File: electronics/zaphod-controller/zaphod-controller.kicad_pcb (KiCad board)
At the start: 4 copper layers, 199.9 x 69.3 mm, 223 parts, among them P1 MOLEX_43160-0102, P11 MOLEX_MINIFIT_JR_2x4_WAY, P12 MOLEX_MINIFIT_JR_2x4_WAY, P13 MOLEX_MINIFIT_JR_2x4_WAY, P14 MOLEX_MINIFIT_JR_2x4_WAY, P15 MOLEX_NANOFIT_2x4_WAY, P17 CONN_01X02, P18 CONN_01X02, P19 CONN_01X02, P2 MOLEX_MINIFIT_JR_2x2_WAY, P20 CONN_01X06, P22 CONN_01X02, P23 MOLEX_KK2.54_1x4_WAY_FAN, P3 MOLEX_MINIFIT_JR_2x2_WAY, P4 MOLEX_MINIFIT_JR_2x2_WAY, P5 MOLEX_MINIFIT_JR_2x2_WAY, Q1 Si7852DP, Q2 Si7852DP, Q3 2N7002P, Q4 NTR1P02T1G, Q5 BC847B, Q6 2N7002P, SW1 B3U-1000P_SPST-NO_SMD, SW2 B3U-1000P_SPST-NO_SMD, SW3 B3U-1000P_SPST-NO_SMD, U1 ISL85410FRZ, U10 ULN2003A, U11 ULN2003A, U2 LM5116, U3 ISL85410FRZ, U4 STM32F429VET6, U5 USBLC6, U6 ACS711KEXLT_15AB, U7 ACS711KEXLT_15AB, U8 ACS711KEXLT_15AB, U9 ACS711KEXLT_15AB, X1 CSTCE8M00G55Z, X2 SWD_SMT_SOCKET, X3 ABS06-107-32.768KHZ

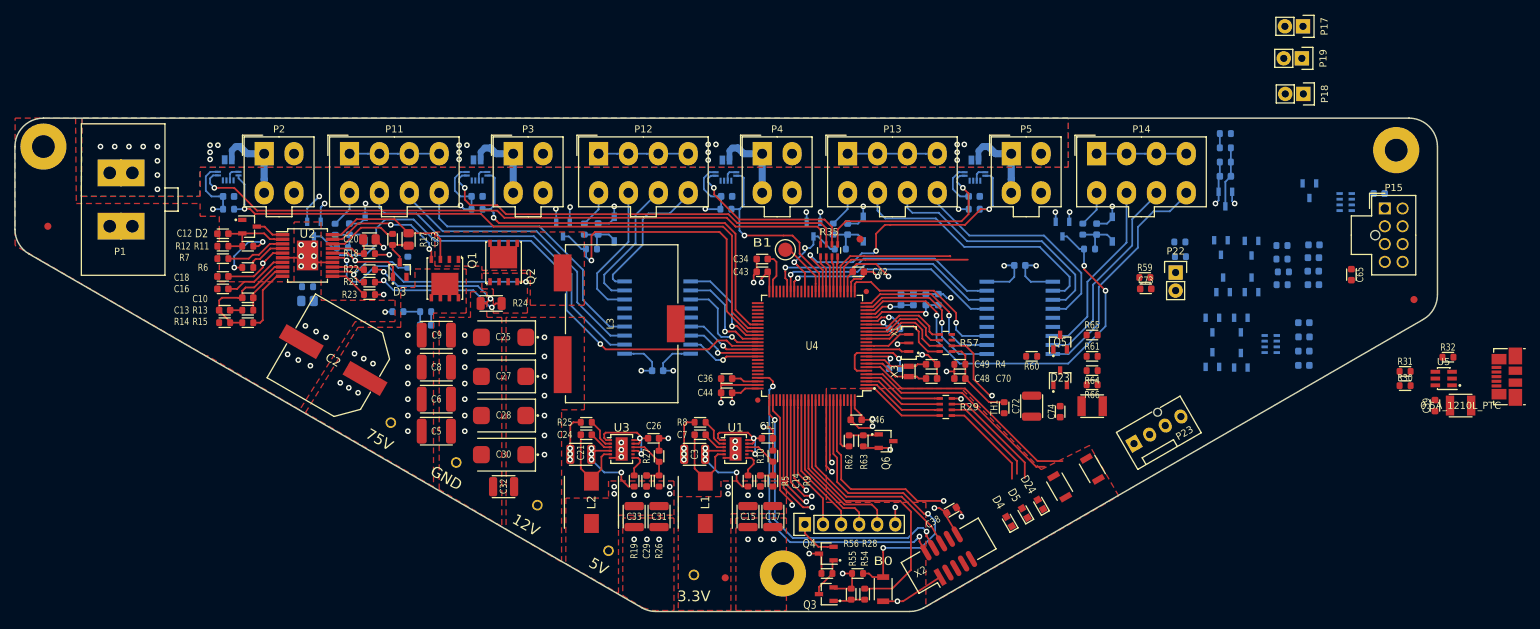
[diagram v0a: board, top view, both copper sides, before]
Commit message: Routing, layout and misc changes
Connectors for IO/Expansion, silkscreen text, misc.
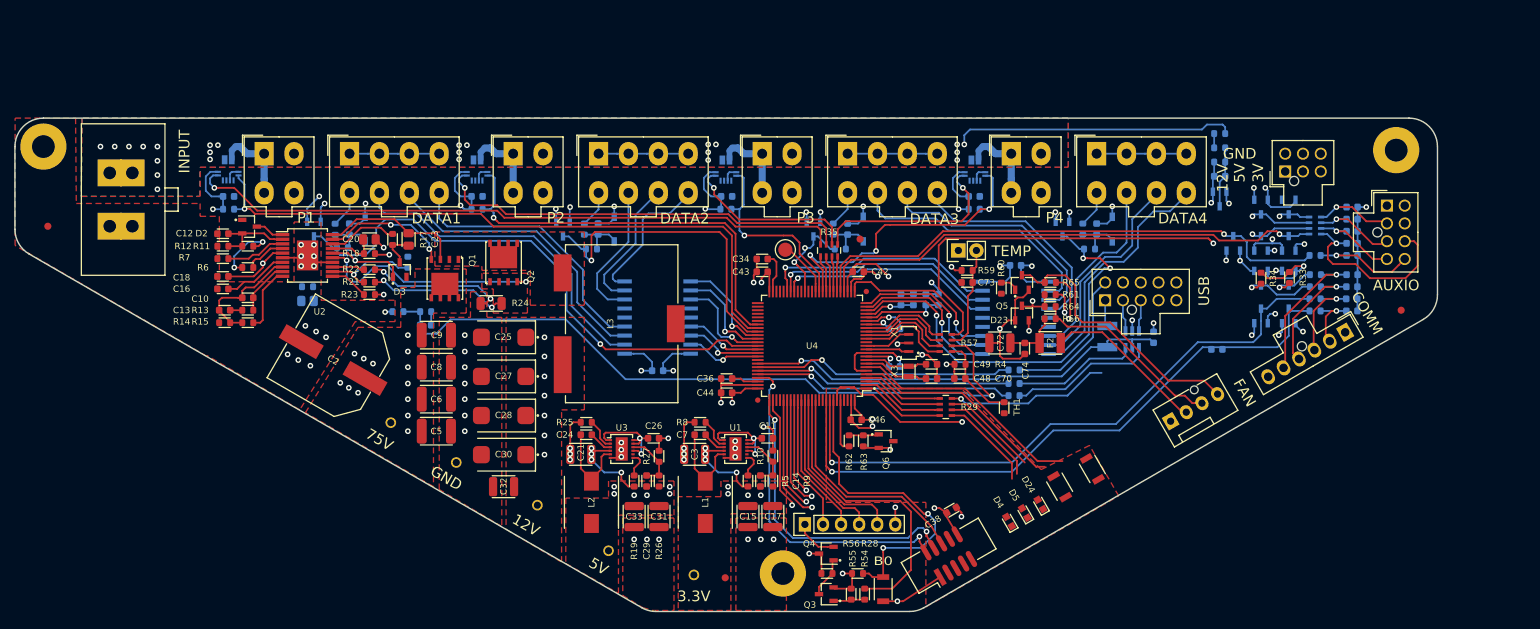
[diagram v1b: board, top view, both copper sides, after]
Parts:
- removed J?1: USB_MICRO_B_SMD_2, Applidyne_USB:MOLEX_47346-0001
- removed P22: CONN_01X02, Applidyne_Connector_Wurth:61300211121
- removed P23: MOLEX_KK2.54_1x4_WAY_FAN, Applidyne_Connector_Molex:MOLEX_47053-1000
- added P16: MOLEX_NANOFIT_1x6_WAY, Applidyne_Connector_Molex:Molex_Nano-Fit_105309-xx06_1x06_VERT, F.Cu at (236.9, 80.1)
- added P21: MOLEX_NANOFIT_2x5_WAY, Applidyne_Connector_Molex:Molex_Nano-Fit_105310-xx10_2x05_VERT, F.Cu at (203.2, 75.6)
- C39, C65, F1, R30, R31, R32, U5: moved to B.Cu
- P17: value CONN_01X02 -> MOLEX_NANOFIT_2x3_WAY; footprint Applidyne_Connector_Wurth:61300211121 -> Applidyne_Connector_Molex:Molex_Nano-Fit_105310-xx06_2x03_VERT
- P19: value CONN_01X02 -> MOLEX_KK2.54_1x4_WAY_FAN; footprint Applidyne_Connector_Wurth:61300211121 -> Applidyne_Connector_Molex:MOLEX_47053-1000
- R33, R34: moved to F.Cu
- R49: value 220R_QUAD_ARRAY_1608M -> 22R_1608M; footprint Applidyne_Resistor:R_Array_Concave_4x1608M -> Applidyne_Resistor:RESC1608X50N
- moved R32 61.0 mm to (190.4, 85.4)
- moved R31 55.1 mm to (190.4, 89.0)
- moved R30 55.0 mm to (190.4, 87.3)
- moved P19 54.2 mm to (212.4, 92.6), turned to 30 degrees
- moved P18 53.2 mm to (182.6, 68.6), turned to 90 degrees
- moved F1 50.6 mm to (203.5, 80.7), turned to 90 degrees
- moved U5 44.1 mm to (207.0, 81.1), turned to 0 degrees
- moved C39 40.7 mm to (210.0, 80.8), turned to 270 degrees
- moved C73 25.1 mm to (183.8, 73.1)
- moved R59 25.0 mm to (183.8, 71.4), turned to 180 degrees
- moved C65 21.6 mm to (218.9, 82.5), turned to 180 degrees
- moved P17 20.6 mm to (228.5, 57.5), turned to 90 degrees
- moved C63 18.4 mm to (237.9, 67.6)
- moved C62 18.2 mm to (237.9, 65.9)
- moved D15 17.9 mm to (225.1, 62.5)
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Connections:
- F1 pad 2: /Processing and Control/USB_IN_VBUS -> LEMO_USB_VBUS
- P17 pad 2: GND -> +5V
- P18 pad 1: +5V -> +3.3V
- P18 pad 2: GND -> Net-(C73-Pad2)
- P19 pad 1: +3.3V -> GND
- P19 pad 2: GND -> Net-(F2-Pad1)
- Q5 pad 3: Net-(P23-Pad4) -> Net-(P19-Pad4)
- R32 pad 2: /Processing and Control/USB_IN_ID -> LEMO_USB_ID
- R49 pad 2: (no net) -> AUX_ANALOG_1
- R64 pad 1: Net-(P23-Pad3) -> Net-(P19-Pad3)
- R65 pad 1: Net-(P23-Pad4) -> Net-(P19-Pad4)
- R66 pad 1: Net-(P23-Pad3) -> Net-(P19-Pad3)
- U5 pad 1: /Processing and Control/USB_IN_D- -> LEMO_USB_D-
- U5 pad 3: /Processing and Control/USB_IN_D+ -> LEMO_USB_D+
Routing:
- net Net-(C71-Pad2): track 14.9 -> 101.5 mm
- net USART_1_TX: track 10.4 -> 89.4 mm
- net USART_1_RX: track 8.89 -> 87.7 mm
- net USB_VBUS: track 0.00 -> 61.1 mm, vias 0 -> 1
- net AUX_ANALOG_1: track 19.6 -> 74.8 mm, vias 0 -> 1
- net GND: track 173.8 -> 228.7 mm, vias 68 -> 81
- net Net-(C1-Pad1): track 8.55 -> 63.0 mm, vias 0 -> 1
- net AUX_ANALOG_0: track 21.3 -> 72.0 mm, vias 0 -> 1
- net +POWER: track 13.2 -> 52.9 mm
- net Net-(P19-Pad4): track 0.00 -> 38.1 mm
- net USB_OTG_ID: track 0.00 -> 36.7 mm, vias 0 -> 1
- net USB_D+: track 0.00 -> 36.5 mm, vias 0 -> 1
- net USB_D-: track 0.00 -> 36.2 mm, vias 0 -> 1
- net +3.3V: track 122.7 -> 156.3 mm, vias 24 -> 31
- net Net-(D23-Pad3): track 1.31 -> 28.8 mm, vias 1 -> 2
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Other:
- board text added: "3V"
- board text added: "AUXIO"
- board text added: "COMM"
- board text added: "DATA1"
- board text added: "DATA2"
- board text added: "DATA3"
- board text added: "DATA4"
- board text added: "DELTA CONTROL S.RAPSON '18"
- board text added: "FAN"
- board text added: "INPUT"
- board text added: "P1"
- board text added: "P2"
- board text added: "P3"
- board text added: "P4"
- board text added: "TEMP"
- board text added: "USB"
- board text removed: "B1"

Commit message: Placed and routed isolation devices, added pours, general routing clean
Starting to look like a finished board, mostly just power pours remaining
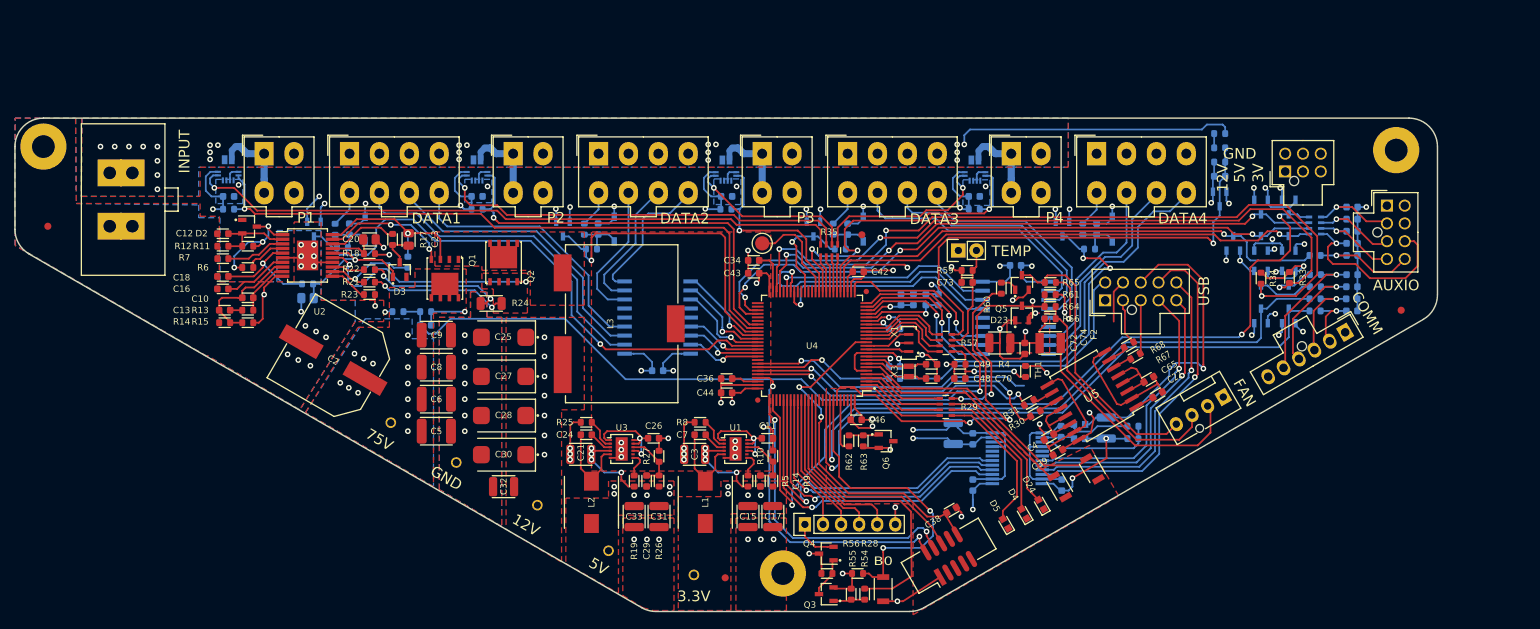
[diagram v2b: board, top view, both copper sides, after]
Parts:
- removed F1: 0.5A_1210L_PTC, Applidyne_Fuse:FUSC3225X85L50N
- added C22: 100n_X7R_1608M, Applidyne_Capacitor:CAPC1608X90N, F.Cu at (210.6, 88.9)
- added C4: 100n_X7R_1608M, Applidyne_Capacitor:CAPC1608X90N, F.Cu at (195.3, 94.8)
- added C75: 10u_X7R_3225M, Applidyne_Capacitor:CAPC3225X170N, B.Cu at (181.8, 94.3)
- added C76: 100n_X7R_1608M, Applidyne_Capacitor:CAPC1608X90N, B.Cu at (184.6, 95.1)
- added C77: 100n_X7R_1608M, Applidyne_Capacitor:CAPC1608X90N, B.Cu at (184.6, 101.6)
- added C78: 100n_X7R_1608M, Applidyne_Capacitor:CAPC1608X90N, B.Cu at (197.1, 101.6)
- added C79: 100n_X7R_1608M, Applidyne_Capacitor:CAPC1608X90N, B.Cu at (197.0, 94.0)
- added C80: 10u_X7R_3225M, Applidyne_Capacitor:CAPC3225X170N, B.Cu at (203.3, 93.5)
- added FB1: 1K_1608M, Applidyne_Inductor:INDC1608X95N, B.Cu at (199.6, 95.0)
- added FB2: 1K_1608M, Applidyne_Inductor:INDC1608X95N, B.Cu at (199.6, 93.0)
- added R67: 22R_1608M, Applidyne_Resistor:RESC1608X50N, F.Cu at (207.5, 83.5)
- added R68: 22R_1608M, Applidyne_Resistor:RESC1608X50N, F.Cu at (206.5, 81.9)
- added R69: 16K9_1608M, Applidyne_Resistor:RESC1608X50N, B.Cu at (207.1, 95.0)
- added R70: 10K0_1608M, Applidyne_Resistor:RESC1608X50N, B.Cu at (207.1, 93.3)
- added U12: ADUM5412, Applidyne_SOP:SOP65P780X200-24L40N, B.Cu at (190.8, 97.8)
- C39, C65, R30, R31: moved to F.Cu
- R49: value 22R_1608M -> 220R_1608M
- U5: value USBLC6 -> ADUM3160; footprint Applidyne_SOT:SOT95P280X145-6L50N -> Applidyne_SOIC:SOIC127P1032X265-16L87N; moved to F.Cu
- moved C39 21.0 mm to (196.5, 97.0), turned to 30 degrees
- moved R32 16.8 mm to (173.6, 86.6)
- moved C65 10.5 mm to (209.3, 86.7), turned to 210 degrees
- moved U5 9.76 mm to (201.3, 89.0), turned to 120 degrees
- moved P19 8.14 mm to (219.8, 89.2), turned to 210 degrees
- moved TH1 5.92 mm to (192.0, 85.6), turned to 270 degrees
- moved R30 5.19 mm to (193.4, 91.5), turned to 210 degrees
- moved TEST8 3.37 mm to (155.0, 67.6)
- moved D5 3.09 mm to (189.2, 107.0)
- moved D4 2.37 mm to (191.8, 105.6)
- moved R31 2.31 mm to (192.5, 90.0), turned to 210 degrees
- moved C34 1.22 mm to (153.8, 70.0)
- moved C43 1.22 mm to (153.8, 71.8)
- moved FID3 0.65 mm to (169.0, 66.4)
- moved C19 0.40 mm to (91.1, 75.3)
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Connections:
- net LEMO_USB_ID renamed ID_SPARE
- C39 pad 2: USB_VBUS -> +3.3V
- C65 pad 1: GND -> ISOLATED_USB_GND
- C65 pad 2: +3.3V -> Net-(C65-Pad2)
- P21 pad 1: LEMO_USB_VBUS -> ISOLATED_USB_GND
- P21 pad 10: Net-(P21-Pad10) -> /Expansion I/O/ISO_OUT_1
- P21 pad 2: LEMO_USB_D- -> ISOLATED_D+
- P21 pad 3: LEMO_USB_D+ -> ISOLATED_D-
- P21 pad 4: Net-(P21-Pad4) -> /Expansion I/O/ISO_IN_1
- P21 pad 5: Net-(P21-Pad5) -> /Expansion I/O/ISO_IN_0
- P21 pad 7: GND -> ISOLATED_USB_VDD
- P21 pad 8: Net-(P21-Pad8) -> /Expansion I/O/ISO_IO_GND
- P21 pad 9: Net-(P21-Pad9) -> /Expansion I/O/ISO_OUT_0
- R30 pad 1: USB_D- -> Net-(R30-Pad1)
- R30 pad 2: Net-(R30-Pad2) -> USB_D-
- R31 pad 1: USB_D+ -> Net-(R31-Pad1)
- R31 pad 2: Net-(R31-Pad2) -> USB_D+
- U5 pad 1: LEMO_USB_D- -> ISOLATED_USB_VDD
- U5 pad 2: GND -> ISOLATED_USB_GND
- U5 pad 3: LEMO_USB_D+ -> Net-(C65-Pad2)
- U5 pad 4: Net-(R31-Pad2) -> Net-(C65-Pad2)
- U5 pad 5: USB_VBUS -> Net-(C65-Pad2)
- U5 pad 6: Net-(R30-Pad2) -> Net-(R67-Pad2)
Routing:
- net I2C_SCK: track 10.8 -> 112.8 mm, vias 1 -> 3
- net AUX_PWM_0: track 20.3 -> 118.9 mm, vias 2 -> 3
- net +5V: track 6.73 -> 104.0 mm, vias 7 -> 8
- net I2C_SDA: track 6.67 -> 101.3 mm, vias 1 -> 3
- net AUX_PWM_1: track 8.55 -> 91.0 mm, vias 1 -> 3
- net AUX_PWM_2: track 8.51 -> 90.9 mm, vias 1 -> 3
- net +12V: track 106.1 -> 172.6 mm, vias 18 -> 20
- net GND: track 228.7 -> 285.5 mm, vias 81 -> 89
- net /Expansion I/O/ISO_OUT_0: track 0.00 -> 50.8 mm, vias 0 -> 1
- net /Expansion I/O/ISO_IO_GND: track 0.00 -> 44.1 mm, vias 0 -> 1
- net /Expansion I/O/ISO_OUT_1: track 0.00 -> 43.6 mm, vias 0 -> 1
- net NRST: track 5.36 -> 48.8 mm, vias 1 -> 2
- net /Expansion I/O/ISO_IN_0: track 0.00 -> 39.5 mm, vias 0 -> 1
- net /Expansion I/O/ISO_IN_1: track 0.00 -> 39.0 mm, vias 0 -> 1
- net EXT_INPUT_1: track 15.6 -> 47.5 mm
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- added copper zone on In2.Cu, net +12V
- added copper zone on In2.Cu, net +5V
- added copper zone on B.Cu, net GND

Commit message: Most routing complete
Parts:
- moved LOGO1 1.17 mm to (181.7, 99.0)
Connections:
- net Net-(P2-Pad1) renamed /Output Circuits and Connectors/M1_PWR
- net Net-(P3-Pad1) renamed /Output Circuits and Connectors/M2_PWR
- net Net-(P4-Pad1) renamed /Output Circuits and Connectors/M3_PWR
- net Net-(P5-Pad1) renamed /Output Circuits and Connectors/M4_PWR
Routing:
- net +POWER: track 55.7 -> 75.1 mm, vias 40 -> 51
- net ISOLATED_USB_VDD: track 8.74 -> 27.9 mm, vias 0 -> 1
- net +12V: track 172.6 -> 186.0 mm, vias 20 -> 22
- net ISOLATED_USB_GND: track 18.2 -> 25.7 mm
- net /Output Circuits and Connectors/M4_PWR: track 12.1 -> 5.50 mm
- net /Output Circuits and Connectors/M1_PWR: track 12.0 -> 5.50 mm
- net /Output Circuits and Connectors/M3_PWR: track 11.9 -> 5.50 mm
- net /Output Circuits and Connectors/M2_PWR: track 11.7 -> 5.50 mm
- net ISOLATED_D+: track 6.50 -> 7.87 mm
- net Net-(D5-PadA): track 20.8 -> 22.1 mm
- net USB_VBUS: track 40.2 -> 39.0 mm
- net ISOLATED_D-: track 7.51 -> 8.46 mm
- net Net-(D4-PadA): track 19.6 -> 20.5 mm
- net SERVO2_EN: track 13.5 -> 14.2 mm
- net SERVO2_B: track 13.0 -> 13.7 mm
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- added copper zone on B.Cu, net +12V
- added copper zone on In2.Cu, net +POWER
- added copper zone on B.Cu, net /Output Circuits and Connectors/M1_PWR
- added copper zone on B.Cu, net /Output Circuits and Connectors/M2_PWR
- added copper zone on B.Cu, net /Output Circuits and Connectors/M3_PWR
- added copper zone on B.Cu, net /Output Circuits and Connectors/M4_PWR
- removed copper zone on In2.Cu, net +12V
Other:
- rule trace_min: 0.2 -> 0.25
- board text added: "A"
- board text added: "B"
- board text added: "C"
- board text added: "INPUT 24-80V"
- board text added: "X"
- board text added: "Y"
- board text removed: "3V"
- board text removed: "AUXIO"
- board text removed: "COMM"
- board text removed: "FAN"
- board text removed: "INPUT"
- board text removed: "USB"

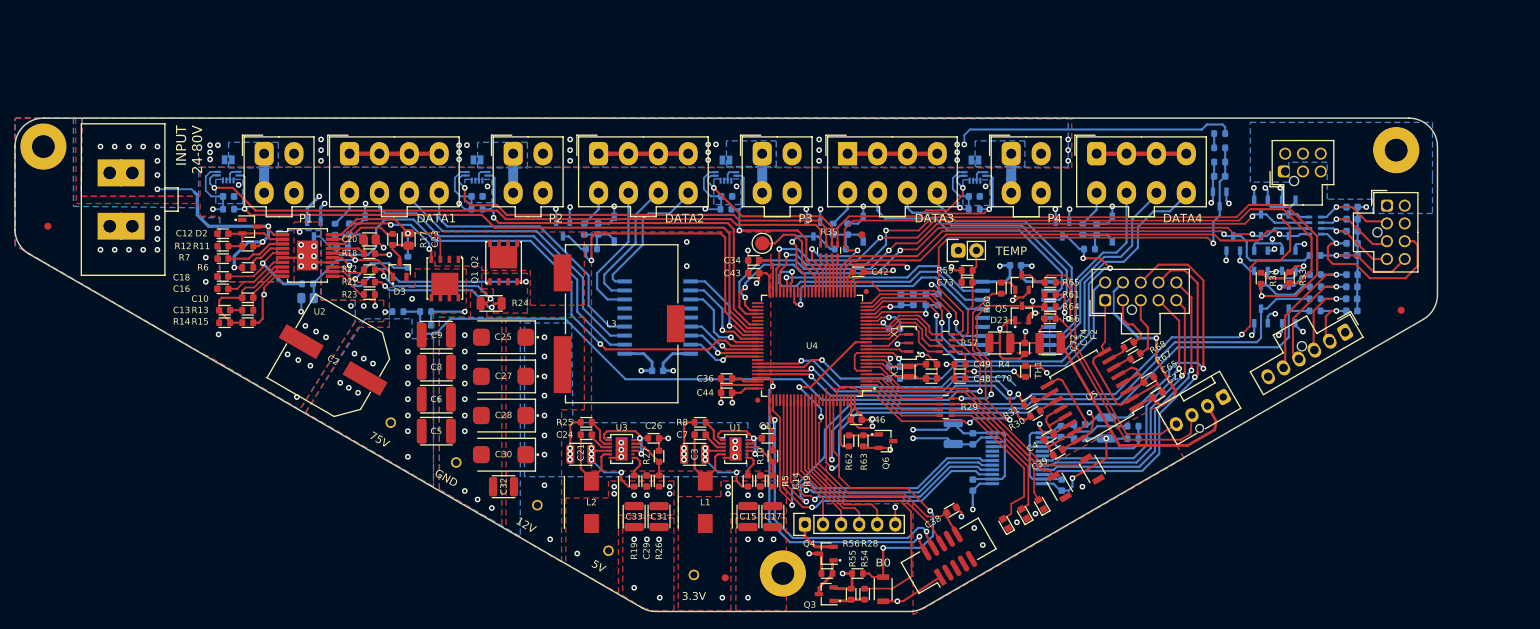
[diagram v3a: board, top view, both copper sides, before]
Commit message: Added sch objects for the additional logo items, finished all routing
Added symbols for HV, temp warning, connectors, etc.
Most pours are now made, played with clearances and internal planes somewhat
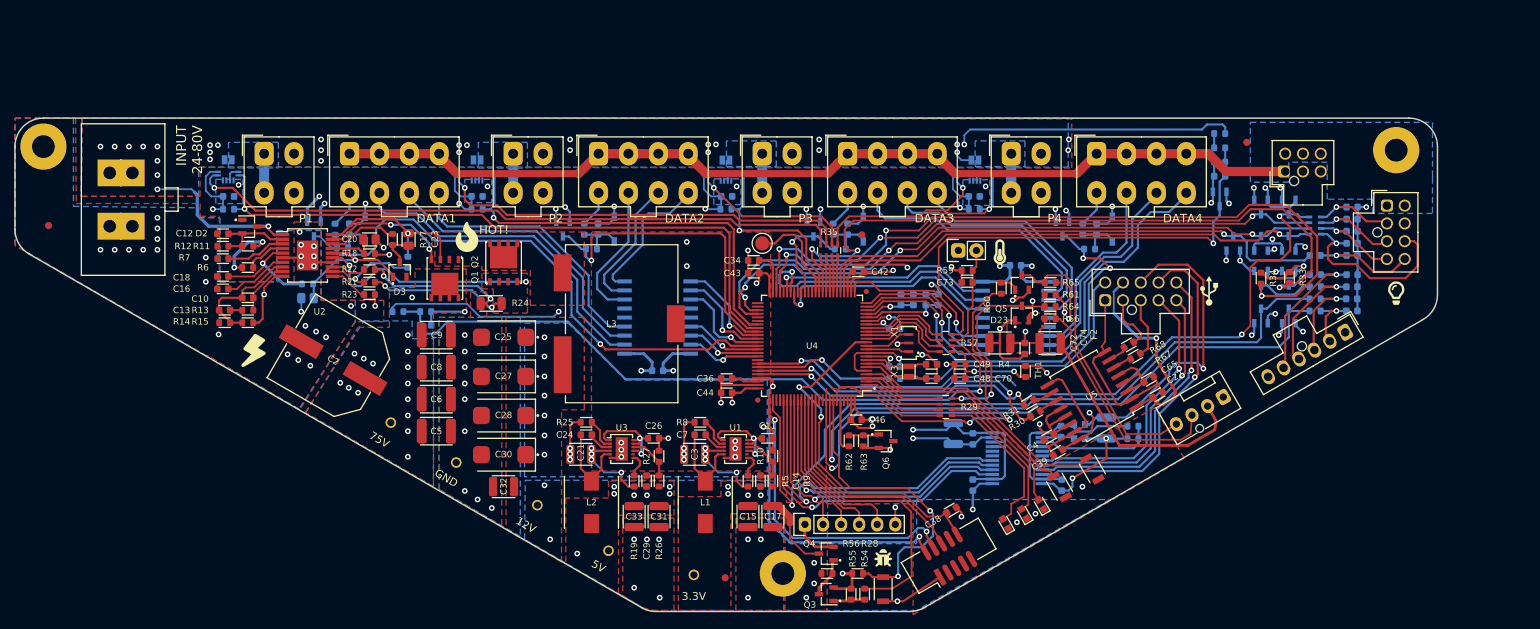
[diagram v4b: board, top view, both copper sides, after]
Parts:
- added LOGO10: LOGO, Applidyne_Logo:WARN_TRIANGLE_LOGO440X400_MASK, B.Cu at (81.6, 81.0)
- added LOGO11: LOGO, Applidyne_Logo:FIRE_LOGO_320X420, F.Cu at (113.5, 66.7)
- added LOGO12: LOGO, Applidyne_Logo:BOLT_LOGO_310X490, F.Cu at (83.5, 83.0)
- added LOGO2: LOGO, Applidyne_Logo:BUG_LOGO250X250, F.Cu at (172.0, 111.8)
- added LOGO3: LOGO, Applidyne_Logo:BULB_LOGO230X330, F.Cu at (244.1, 74.6)
- added LOGO4: LOGO, Applidyne_Logo:THERMO_LOGO_170X350, F.Cu at (188.4, 68.8)
- added LOGO5: LOGO, Applidyne_Logo:USB_LOGO410X250, F.Cu at (217.8, 74.3)
- added LOGO6: LOGO, Applidyne_Logo:WARN_TRIANGLE_LOGO440X400, B.Cu at (192.2, 65.1)
- added LOGO7: LOGO, Applidyne_Logo:WARN_TRIANGLE_LOGO440X400, B.Cu at (122.1, 65.1)
- added LOGO8: LOGO, Applidyne_Logo:WARN_TRIANGLE_LOGO440X400, B.Cu at (87.1, 65.1)
- added LOGO9: LOGO, Applidyne_Logo:WARN_TRIANGLE_LOGO440X400, B.Cu at (157.2, 65.1)
- moved FID4 32.1 mm to (223.1, 53.4)
- moved FID1 0.14 mm to (54.7, 65.1)
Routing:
- net +12V: track 186.0 -> 338.1 mm
- net +5V: track 104.0 -> 165.4 mm
- net +3.3V: track 179.7 -> 210.9 mm, vias 35 -> 36
- net +POWER: track 75.1 -> 77.8 mm, vias 51 -> 48
- net BOOT0: track 44.4 -> 43.9 mm
- net GND: track 285.1 -> 284.9 mm, vias 120 -> 112
- added copper zone on B.Cu, net +3.3V
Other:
- board text added: "HOT!"
- board text added: "WARNING 75V PRESENT"
- board text removed: "B0"
- board text removed: "TEMP"
